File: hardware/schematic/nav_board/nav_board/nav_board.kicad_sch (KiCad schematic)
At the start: 7 parts, among them J1 RS232 to Display, J2 Flow Meter, J3 Depth Sensor, J4 Picoblade to GPS

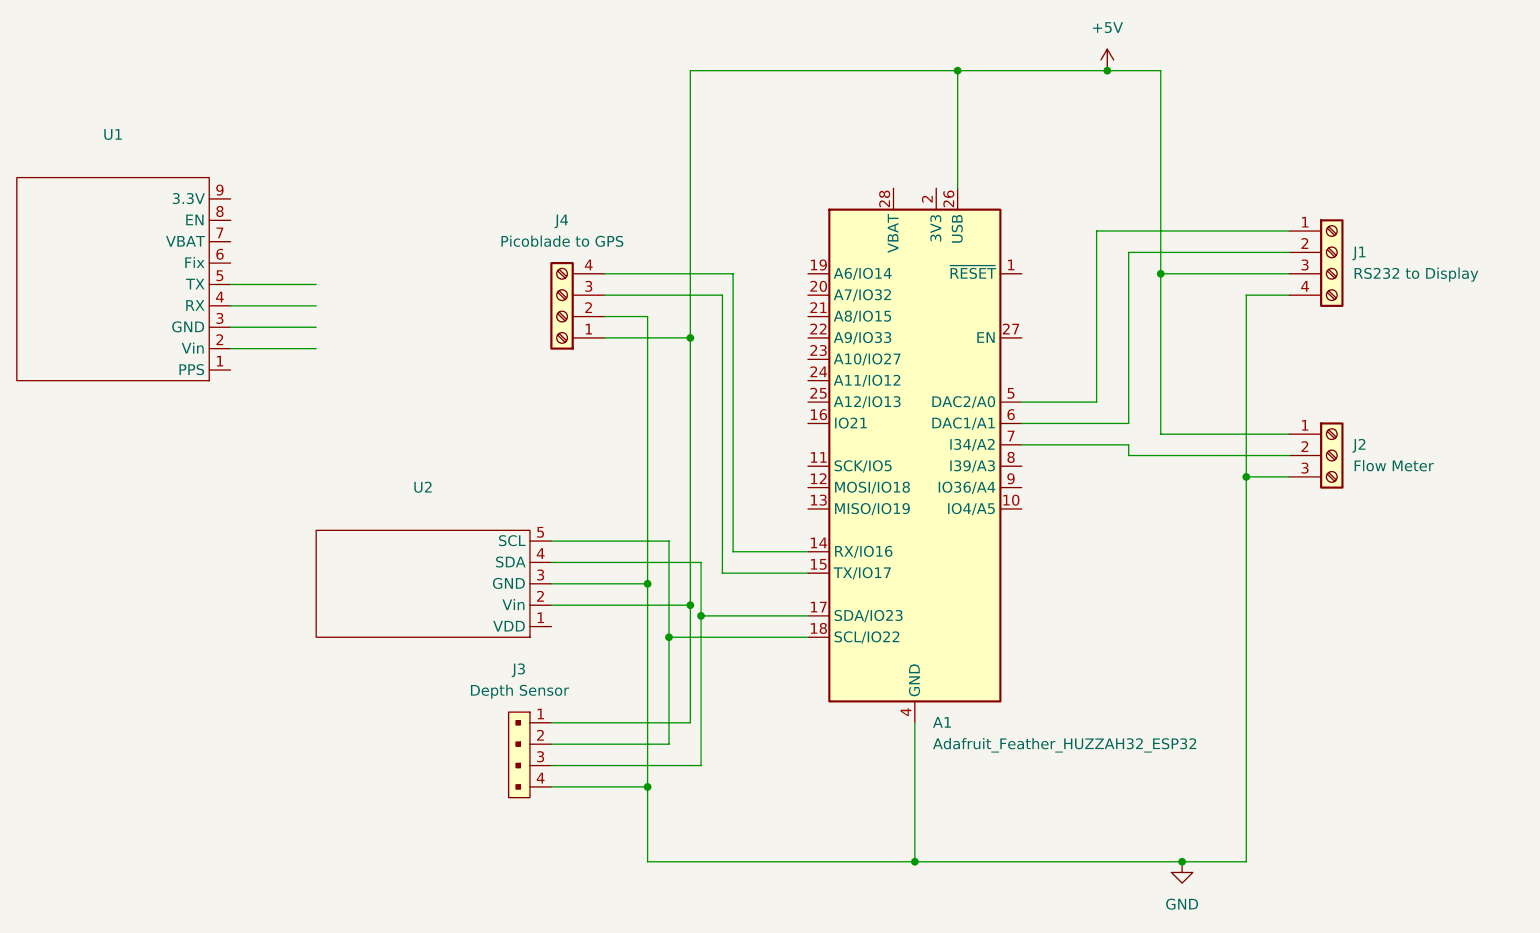
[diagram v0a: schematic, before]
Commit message: Consolidate display_board/nav_board KiCad files to latest local work
This machine has the most recent hardware design work. Promote the
Rev B design to canonical display_board.kicad_pro/.kicad_sch/.kicad_pcb,
move its matching gerbers/drill files into manufacturing/, track the
gopro-housing variant as a maintained alternate board, and drop the
superseded Rev A files, stale fabrication/ output, and backup zips
(archived locally under a gitignored _archive/ folder rather than
deleted outright). Also brings nav_board's schematic/PCB/manufacturing
files up to date.

Co-Authored-By: Claude Sonnet 5 <noreply@anthropic.com>
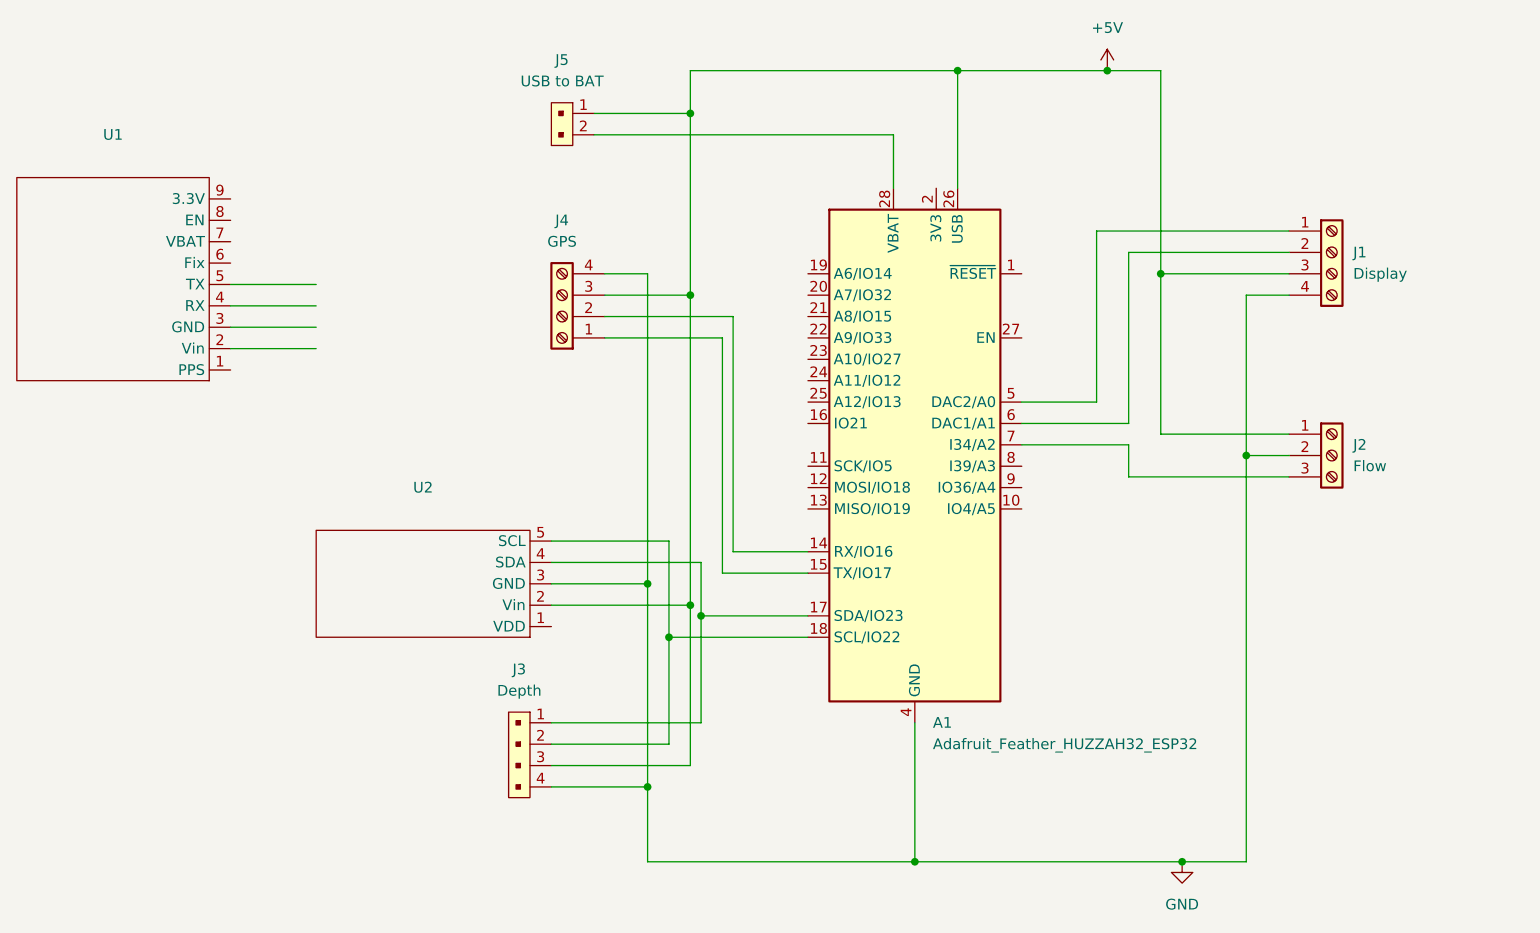
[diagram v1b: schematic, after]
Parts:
- added J5: USB to BAT, digikey-footprints:PinHeader_1x2_P2.54mm_Drill1.02mm, symbol dk_Rectangular-Connectors-Headers-Male-Pins:22-23-2021
- J1: value RS232 to Display -> Display
- J2: value Flow Meter -> Flow
- J3: value Depth Sensor -> Depth
- J4: value Picoblade to GPS -> GPS
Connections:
- net +5V: now also J3.3, J4.3 (Pin_3), J5.1; no longer J3.1, J4.1 (Pin_1)
- net GND: now also J2.2 (Pin_2), J4.4 (Pin_4); no longer J2.3 (Pin_3), J4.2 (Pin_2)
- net at A1.15 (TX/IO17): now also J4.1 (Pin_1); no longer J4.3 (Pin_3)
- net at A1.14 (RX/IO16): now also J4.2 (Pin_2); no longer J4.4 (Pin_4)
- net at A1.17 (SDA/IO23), U2.4 (SDA): now also J3.1; no longer J3.3
- net at A1.28 (VBAT): now also J5.2
- net at A1.7 (I34/A2): now also J2.3 (Pin_3); no longer J2.2 (Pin_2)
